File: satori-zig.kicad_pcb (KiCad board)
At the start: 2 copper layers, 30 x 22.5 mm, 2 parts

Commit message: Input Net name
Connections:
- net Net-(CN1-Pad17) renamed /RX
- net Net-(CN1-Pad19) renamed /TX
- net Net-(CN1-Pad20) renamed /WAKE
- net Net-(CN1-Pad3) renamed /RESET

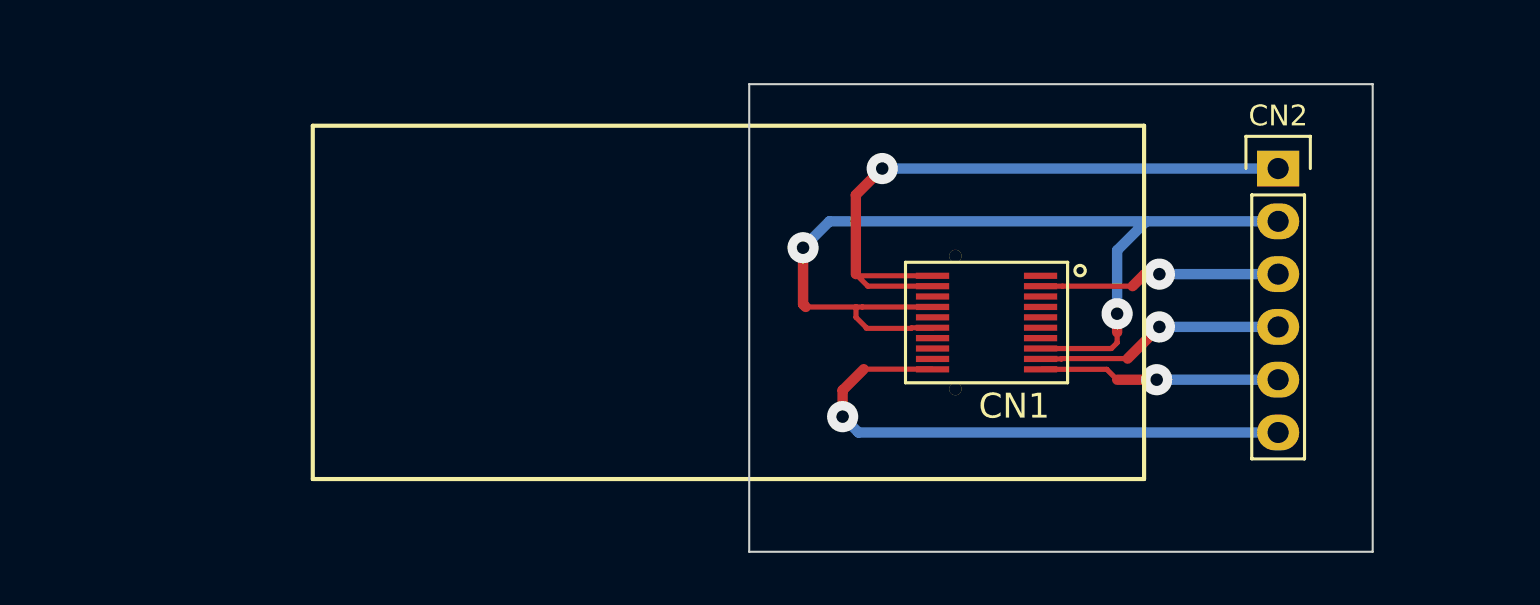
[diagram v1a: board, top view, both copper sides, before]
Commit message: ドリル穴等の配置
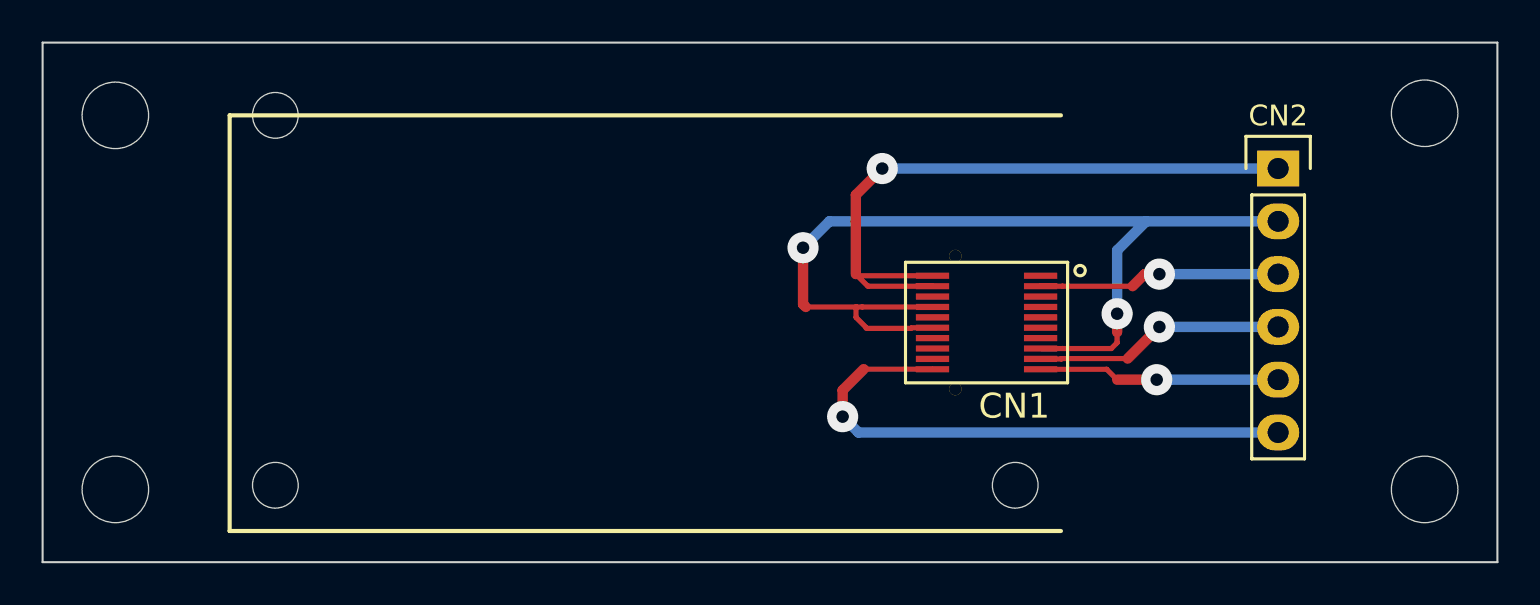
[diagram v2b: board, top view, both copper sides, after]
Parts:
- added REF**: MountingHole_2.2mm_M2, Mounting_Holes:MountingHole_2.2mm_M2, F.Cu at (158.8, 114.3)
- added REF**: MountingHole_2.2mm_M2, Mounting_Holes:MountingHole_2.2mm_M2, F.Cu at (123.2, 114.3)
- added REF**: MountingHole_2.2mm_M2, Mounting_Holes:MountingHole_2.2mm_M2, F.Cu at (123.2, 96.5)
- added REF**: MountingHole_3.2mm_M3, Mounting_Holes:MountingHole_3.2mm_M3, F.Cu at (178.5, 114.5)
- added REF**: MountingHole_3.2mm_M3, Mounting_Holes:MountingHole_3.2mm_M3, F.Cu at (178.5, 96.4)
- added REF**: MountingHole_3.2mm_M3, Mounting_Holes:MountingHole_3.2mm_M3, F.Cu at (115.5, 96.5)
- added REF**: MountingHole_3.2mm_M3, Mounting_Holes:MountingHole_3.2mm_M3, F.Cu at (115.5, 114.5)
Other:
- board size 30 x 22.5 mm -> 70 x 25 mm

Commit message: ドリル穴位置修正
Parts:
- moved REF** 2.20 mm to (123.2, 98.7)
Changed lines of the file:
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@@
   )
   (module Mounting_Holes:MountingHole_2.2mm_M2 (layer F.Cu)
-    (at 123.2 96.5)
+    (at 123.2 98.7)
     (descr "Mounting Hole 2.2mm, no annular, M2")
     (tags "mounting hole 2.2mm no annular m2")

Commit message: 取り付け穴減らす
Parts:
- removed the REF** at (123.2, 114.3)
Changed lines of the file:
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@@
     (tracks 56)
     (zones 0)
-    (modules 9)
+    (modules 8)
     (nets 18)
   )
@@
     (pad 22 thru_hole circle (at 3.2 1.5 270) (size 0.6 0.6) (drill 0.6) (layers *.Cu *.Mask)
       (zone_connect 0))
+    (pad 23 smd rect (at 3.9 0 270) (size 0.8 2) (layers F.Cu F.Paste F.Mask))
+    (pad 24 smd rect (at -3.9 0 270) (size 0.8 2) (layers F.Cu F.Paste F.Mask))
   )
   (module Pin_Headers:Pin_Header_Straight_1x06 (layer F.Cu)
@@
     (descr "Mounting Hole 2.2mm, no annular, M2")
     (tags "mounting hole 2.2mm no annular m2")
-    (fp_text reference REF** (at 0 -3.2) (layer F.SilkS) hide
-      (effects (font (size 1 1) (thickness 0.15)))
-    )
-    (fp_text value MountingHole_2.2mm_M2 (at 0 3.2) (layer F.Fab) hide
-      (effects (font (size 1 1) (thickness 0.15)))
-    )
-    (fp_circle (center 0 0) (end 2.2 0) (layer Cmts.User) (width 0.15))
-    (fp_circle (center 0 0) (end 2.45 0) (layer F.CrtYd) (width 0.05))
-    (pad 1 np_thru_hole circle (at 0 0) (size 2.2 2.2) (drill 2.2) (layers *.Cu *.Mask))
-  )
-  (module Mounting_Holes:MountingHole_2.2mm_M2 (layer F.Cu)
-    (at 123.2 114.3)
-    (descr "Mounting Hole 2.2mm, no annular, M2")
-    (tags "mounting hole 2.2mm no annular m2")
